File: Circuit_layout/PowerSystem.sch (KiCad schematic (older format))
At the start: 21 parts, among them U13 PDQ10-D, U14 PDQ15-D, U18 PDQ6-D

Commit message: fixed the throttle.
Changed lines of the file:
@@
 	5400 3650 5300 3650
 Wire Wire Line
-	5300 3550 5300 3650
-Wire Wire Line
-	4100 3550 5300 3550
+	5300 3650 5300 3550
+Wire Wire Line
+	5300 3550 4100 3550
 Connection ~ 4950 3550
 Connection ~ 4550 3550
@@
 	5400 3750 5300 3750
 Wire Wire Line
-	5300 3850 5300 3750
-Wire Wire Line
-	4100 3850 5300 3850
+	5300 3750 5300 3850
+Wire Wire Line
+	5300 3850 4100 3850
 Connection ~ 4950 3850
 Connection ~ 4550 3850
@@
 	5400 1600 5250 1600
 Wire Wire Line
-	5250 1550 5250 1600
+	5250 1600 5250 1550
 Wire Wire Line
 	5400 1700 5250 1700
 Wire Wire Line
-	5250 1850 5250 1700
-Wire Wire Line
-	4100 1850 5250 1850
+	5250 1700 5250 1850
+Wire Wire Line
+	5250 1850 4100 1850
 Connection ~ 4900 1550
 Connection ~ 4900 1850
@@
 Connection ~ 4550 1550
 $Comp
-L +24V #PWR43
+L +24V #PWR044
 U 1 1 58AF1DB3
 P 4100 3550
-F 0 "#PWR43" H 4100 3400 50  0001 C CNN
+F 0 "#PWR044" H 4100 3400 50  0001 C CNN
 F 1 "+24V" H 4100 3690 50  0000 C CNN
 F 2 "" H 4100 3550 50  0000 C CNN
@@
 $EndComp
 $Comp
-L +24V #PWR42
+L +24V #PWR045
 U 1 1 58AF1DD3
 P 4100 1550
-F 0 "#PWR42" H 4100 1400 50  0001 C CNN
+F 0 "#PWR045" H 4100 1400 50  0001 C CNN
 F 1 "+24V" H 4100 1690 50  0000 C CNN
 F 2 "" H 4100 1550 50  0000 C CNN
@@
 	7300 1600 7300 1500
 $Comp
-L +5V #PWR45
+L +5V #PWR046
 U 1 1 58AF2067
 P 7300 1500
-F 0 "#PWR45" H 7300 1350 50  0001 C CNN
+F 0 "#PWR046" H 7300 1350 50  0001 C CNN
 F 1 "+5V" H 7300 1640 50  0000 C CNN
 F 2 "" H 7300 1500 50  0000 C CNN
@@
 $EndComp
 $Comp
-L +12V #PWR47
+L +12V #PWR047
 U 1 1 58AF208D
 P 7350 3550
-F 0 "#PWR47" H 7350 3400 50  0001 C CNN
+F 0 "#PWR047" H 7350 3400 50  0001 C CNN
 F 1 "+12V" H 7350 3690 50  0000 C CNN
 F 2 "" H 7350 3550 50  0000 C CNN
@@
 	7300 1800 7300 1900
 $Comp
-L GND #PWR46
+L GND #PWR048
 U 1 1 58AF2561
 P 7300 1900
-F 0 "#PWR46" H 7300 1650 50  0001 C CNN
+F 0 "#PWR048" H 7300 1650 50  0001 C CNN
 F 1 "GND" H 7300 1750 50  0000 C CNN
 F 2 "" H 7300 1900 50  0000 C CNN
@@
 	7350 3850 7350 4000
 $Comp
-L GND #PWR48
+L GND #PWR049
 U 1 1 58AF25AA
 P 7350 4000
-F 0 "#PWR48" H 7350 3750 50  0001 C CNN
+F 0 "#PWR049" H 7350 3750 50  0001 C CNN
 F 1 "GND" H 7350 3850 50  0000 C CNN
 F 2 "" H 7350 4000 50  0000 C CNN
@@
 	4000 6900 3900 6900
 Wire Wire Line
-	3900 6800 3900 6900
-Wire Wire Line
-	3500 6800 3900 6800
+	3900 6900 3900 6800
+Wire Wire Line
+	3900 6800 3500 6800
 Connection ~ 3700 6800
 Connection ~ 3700 7100
@@
 LV_RTN
 $Comp
-L GND #PWR44
+L GND #PWR050
 U 1 1 58BA25F0
 P 6700 7250
-F 0 "#PWR44" H 6700 7000 50  0001 C CNN
+F 0 "#PWR050" H 6700 7000 50  0001 C CNN
 F 1 "GND" H 6700 7100 50  0000 C CNN
 F 2 "" H 6700 7250 50  0000 C CNN
@@
 	6700 7150 6700 7250
 Wire Wire Line
-	4100 1550 5250 1550
+	5250 1550 4100 1550
 Wire Notes Line
 	4750 6300 4750 7800
@@
 $EndComp
 $Comp
-L GND #PWR52
+L GND #PWR051
 U 1 1 58B9D18E
 P 7850 1950
-F 0 "#PWR52" H 7850 1700 50  0001 C CNN
+F 0 "#PWR051" H 7850 1700 50  0001 C CNN
 F 1 "GND" H 7850 1800 50  0000 C CNN
 F 2 "" H 7850 1950 50  0000 C CNN
@@
 $EndComp
 $Comp
-L +5V #PWR51
+L +5V #PWR052
 U 1 1 58B9D1D5
 P 7850 1450
-F 0 "#PWR51" H 7850 1300 50  0001 C CNN
+F 0 "#PWR052" H 7850 1300 50  0001 C CNN
 F 1 "+5V" H 7850 1590 50  0000 C CNN
 F 2 "" H 7850 1450 50  0000 C CNN
@@
 $EndComp
 $Comp
-L GND #PWR50
+L GND #PWR053
 U 1 1 58B9D3A5
 P 7750 4050
-F 0 "#PWR50" H 7750 3800 50  0001 C CNN
+F 0 "#PWR053" H 7750 3800 50  0001 C CNN
 F 1 "GND" H 7750 3900 50  0000 C CNN
 F 2 "" H 7750 4050 50  0000 C CNN
@@
 	7750 4050 7750 3950
 $Comp
-L +12V #PWR49
+L +12V #PWR054
 U 1 1 58B9D62A
 P 7750 3300
-F 0 "#PWR49" H 7750 3150 50  0001 C CNN
+F 0 "#PWR054" H 7750 3150 50  0001 C CNN
 F 1 "+12V" H 7750 3440 50  0000 C CNN
 F 2 "" H 7750 3300 50  0000 C CNN
@@
 $EndComp
 $Comp
-L PWR_FLAG #FLG3
+L PWR_FLAG #FLG055
 U 1 1 58B9E33D
 P 8150 3300
-F 0 "#FLG3" H 8150 3395 50  0001 C CNN
+F 0 "#FLG055" H 8150 3395 50  0001 C CNN
 F 1 "PWR_FLAG" H 8150 3480 50  0000 C CNN
 F 2 "" H 8150 3300 50  0000 C CNN

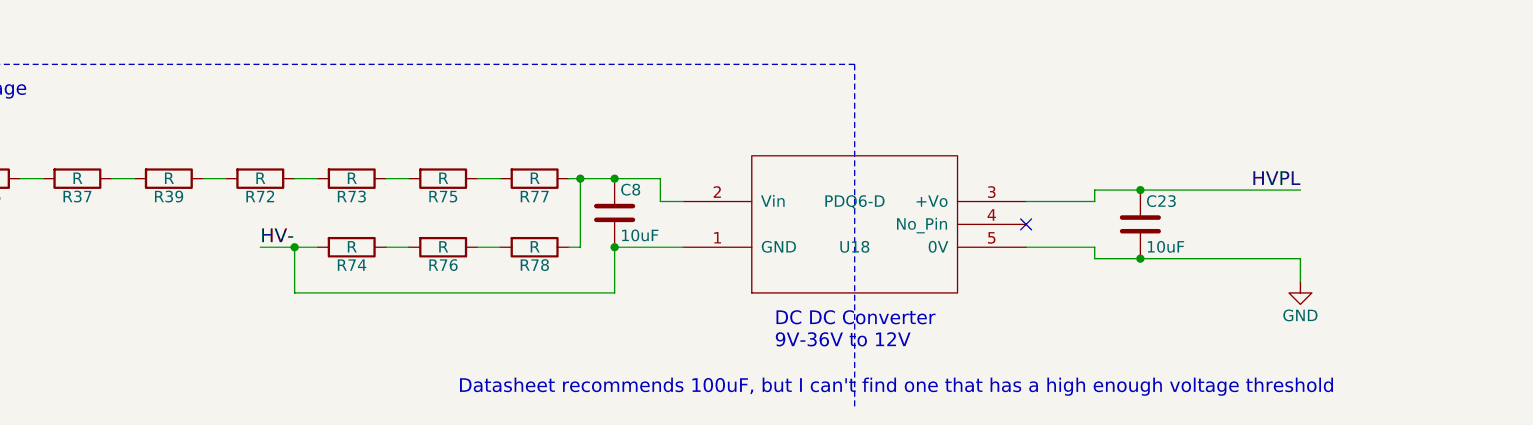
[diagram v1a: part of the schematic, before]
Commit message: added footprints
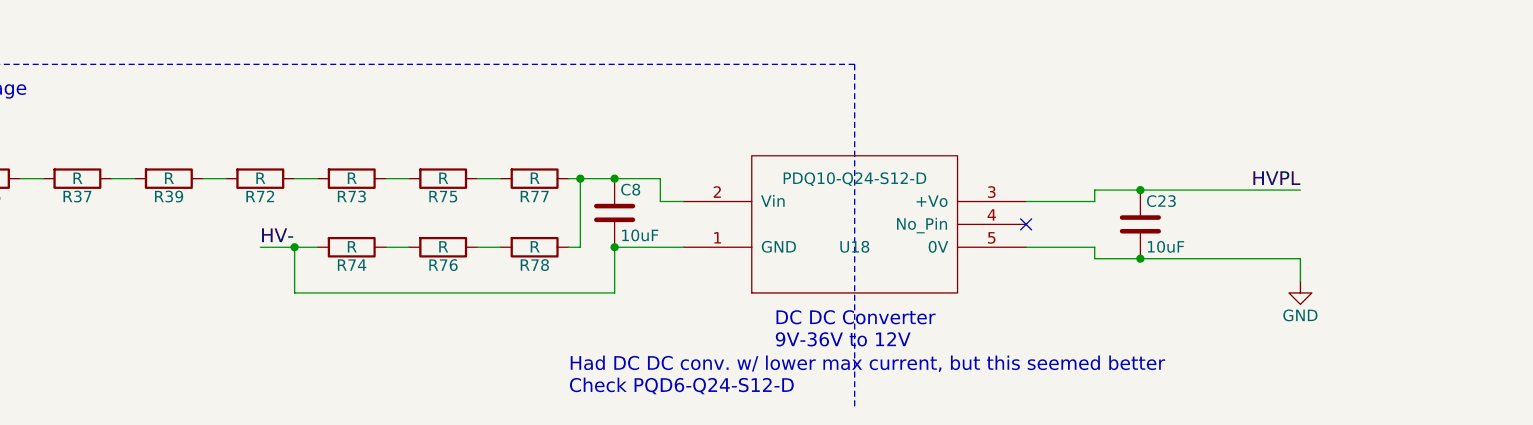
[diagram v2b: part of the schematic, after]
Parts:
- U13, U14: footprint (none) -> custom_footprints:PDQ_DCDC
- U18: value PDQ6-D -> PDQ10-Q24-S12-D; footprint (none) -> custom_footprints:PDQ_DCDC; DigiKey P/N  (none) -> 102-3866-ND; Man P/N (none) -> PDQ10-Q24-S12-D; URL (none) -> http://www.digikey.com/product-detail/en/cui-inc/PDQ10-Q24-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
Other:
- note added: "Had DC DC conv. w/ lower max current, but this seemed better\nCheck PQD6-Q24-S12-D"
- note removed: "Datasheet recommends 100uF, but I can't find one that has a high enough voltage threshold"
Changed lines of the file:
@@
 EESchema Schematic File Version 2
 LIBS:Circuit_layout-rescue
+LIBS:TSI_KiCad_Lib
 LIBS:TSI_HV_Isolater-cache
 LIBS:74xgxx
@@
 F 0 "U13" H 6150 1600 50  0000 C CNN
 F 1 "PDQ10-D" H 6150 1800 50  0000 C CNN
-F 2 "" H 6150 1300 50  0001 C CNN
+F 2 "custom_footprints:PDQ_DCDC" H 6150 1300 50  0001 C CNN
 F 3 "" H 6150 1200 50  0001 C CNN
 F 4 "	102-3865-ND" H 6150 1700 60  0001 C CNN "DigiKey P/N"
@@
 F 0 "U14" H 6150 3650 50  0000 C CNN
 F 1 "PDQ15-D" H 6150 3850 50  0000 C CNN
-F 2 "" H 6150 3350 50  0001 C CNN
+F 2 "custom_footprints:PDQ_DCDC" H 6150 3350 50  0001 C CNN
 F 3 "" H 6150 3250 50  0001 C CNN
 F 4 "102-3880-ND" H 6150 3750 60  0001 C CNN "DigiKey P/N"
@@
 Connection ~ 4550 1550
 $Comp
-L +24V #PWR044
+L +24V #PWR43
 U 1 1 58AF1DB3
 P 4100 3550
-F 0 "#PWR044" H 4100 3400 50  0001 C CNN
+F 0 "#PWR43" H 4100 3400 50  0001 C CNN
 F 1 "+24V" H 4100 3690 50  0000 C CNN
 F 2 "" H 4100 3550 50  0000 C CNN
@@
 $EndComp
 $Comp
-L +24V #PWR045
+L +24V #PWR42
 U 1 1 58AF1DD3
 P 4100 1550
-F 0 "#PWR045" H 4100 1400 50  0001 C CNN
+F 0 "#PWR42" H 4100 1400 50  0001 C CNN
 F 1 "+24V" H 4100 1690 50  0000 C CNN
 F 2 "" H 4100 1550 50  0000 C CNN
@@
 	7300 1600 7300 1500
 $Comp
-L +5V #PWR046
+L +5V #PWR45
 U 1 1 58AF2067
 P 7300 1500
-F 0 "#PWR046" H 7300 1350 50  0001 C CNN
+F 0 "#PWR45" H 7300 1350 50  0001 C CNN
 F 1 "+5V" H 7300 1640 50  0000 C CNN
 F 2 "" H 7300 1500 50  0000 C CNN
@@
 $EndComp
 $Comp
-L +12V #PWR047
+L +12V #PWR47
 U 1 1 58AF208D
 P 7350 3550
-F 0 "#PWR047" H 7350 3400 50  0001 C CNN
+F 0 "#PWR47" H 7350 3400 50  0001 C CNN
 F 1 "+12V" H 7350 3690 50  0000 C CNN
 F 2 "" H 7350 3550 50  0000 C CNN
@@
 	7300 1800 7300 1900
 $Comp
-L GND #PWR048
+L GND #PWR46
 U 1 1 58AF2561
 P 7300 1900
-F 0 "#PWR048" H 7300 1650 50  0001 C CNN
+F 0 "#PWR46" H 7300 1650 50  0001 C CNN
 F 1 "GND" H 7300 1750 50  0000 C CNN
 F 2 "" H 7300 1900 50  0000 C CNN
@@
 	7350 3850 7350 4000
 $Comp
-L GND #PWR049
+L GND #PWR48
 U 1 1 58AF25AA
 P 7350 4000
-F 0 "#PWR049" H 7350 3750 50  0001 C CNN
+F 0 "#PWR48" H 7350 3750 50  0001 C CNN
 F 1 "GND" H 7350 3850 50  0000 C CNN
 F 2 "" H 7350 4000 50  0000 C CNN
@@
 P 4750 7000
 F 0 "U18" H 4750 6900 50  0000 C CNN
-F 1 "PDQ6-D" H 4750 7100 50  0000 C CNN
-F 2 "" H 4750 6600 50  0001 C CNN
+F 1 "PDQ10-Q24-S12-D" H 4750 7200 50  0000 C CNN
+F 2 "custom_footprints:PDQ_DCDC" H 4750 6600 50  0001 C CNN
 F 3 "" H 4750 6500 50  0001 C CNN
+F 4 "102-3866-ND" H 4750 7000 60  0001 C CNN "DigiKey P/N "
+F 5 "http://www.digikey.com/product-detail/en/cui-inc/PDQ10-Q24-S12-D/102-3866-ND/6165207" H 4750 7000 60  0001 C CNN "URL"
+F 6 "PDQ10-Q24-S12-D" H 4750 7000 60  0001 C CNN "Man P/N"
 	1    4750 7000
 	1    0    0    -1
@@
 	1    0    0    -1
 $EndComp
-Text Notes 6850 7750 2    60   ~ 0
-Datasheet recommends 100uF, but I can't find one that has a high enough voltage threshold
+Text Notes 3500 7750 0    60   ~ 0
+Had DC DC conv. w/ lower max current, but this seemed better\nCheck PQD6-Q24-S12-D
 $Comp
 L C C10
@@
 LV_RTN
 $Comp
-L GND #PWR050
+L GND #PWR44
 U 1 1 58BA25F0
 P 6700 7250
-F 0 "#PWR050" H 6700 7000 50  0001 C CNN
+F 0 "#PWR44" H 6700 7000 50  0001 C CNN
 F 1 "GND" H 6700 7100 50  0000 C CNN
 F 2 "" H 6700 7250 50  0000 C CNN
@@
 $EndComp
 $Comp
-L GND #PWR051
+L GND #PWR52
 U 1 1 58B9D18E
 P 7850 1950
-F 0 "#PWR051" H 7850 1700 50  0001 C CNN
+F 0 "#PWR52" H 7850 1700 50  0001 C CNN
 F 1 "GND" H 7850 1800 50  0000 C CNN
 F 2 "" H 7850 1950 50  0000 C CNN
@@
 $EndComp
 $Comp
-L +5V #PWR052
+L +5V #PWR51
 U 1 1 58B9D1D5
 P 7850 1450
-F 0 "#PWR052" H 7850 1300 50  0001 C CNN
+F 0 "#PWR51" H 7850 1300 50  0001 C CNN
 F 1 "+5V" H 7850 1590 50  0000 C CNN
 F 2 "" H 7850 1450 50  0000 C CNN
@@
 $EndComp
 $Comp
-L GND #PWR053
+L GND #PWR50
 U 1 1 58B9D3A5
 P 7750 4050
-F 0 "#PWR053" H 7750 3800 50  0001 C CNN
+F 0 "#PWR50" H 7750 3800 50  0001 C CNN
 F 1 "GND" H 7750 3900 50  0000 C CNN
 F 2 "" H 7750 4050 50  0000 C CNN
@@
 	7750 4050 7750 3950
 $Comp
-L +12V #PWR054
+L +12V #PWR49
 U 1 1 58B9D62A
 P 7750 3300
-F 0 "#PWR054" H 7750 3150 50  0001 C CNN
+F 0 "#PWR49" H 7750 3150 50  0001 C CNN
 F 1 "+12V" H 7750 3440 50  0000 C CNN
 F 2 "" H 7750 3300 50  0000 C CNN
@@
 $EndComp
 $Comp
-L PWR_FLAG #FLG055
+L PWR_FLAG #FLG3
 U 1 1 58B9E33D
 P 8150 3300
-F 0 "#FLG055" H 8150 3395 50  0001 C CNN
+F 0 "#FLG3" H 8150 3395 50  0001 C CNN
 F 1 "PWR_FLAG" H 8150 3480 50  0000 C CNN
 F 2 "" H 8150 3300 50  0000 C CNN

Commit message: changing hvpl
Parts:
- removed R36, R37, R39, R72, R73, R74, R75, R76, R77, R78: R, symbol R
- added C?: 10uF, Capacitors_SMD:C_0805_HandSoldering, symbol C
- added L?: INDUCTOR, symbol INDUCTOR
- added R? (x4): R, symbol R
- added U?: LTC3638, custom_footprints:TSSOP16_LTC3638, symbol LTC3638
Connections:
- net HV+: now also C?.1, R?.1, U?.3 (Vin)
- net HV-: now also C?.2, R?.2, R?.2, U?.12 (OVLO), U?.16 (GND), U?.17 (GND), U?.6 (VPRG2), U?.8 (GND); no longer C8.2, U18.1 (GND)
- new net: C8.2, U18.1 (GND)
- new net: L?.1, U?.1 (SW)
- new net: U?.10 (SS), U?.7 (VPRG1)
- new net: R?.1, R?.2, U?.14 (RUN)
- new net: R?.1, R?.2, U?.9 (VFB)
- new net: L?.2, R?.1
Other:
- note removed: "Had DC DC conv. w/ lower max current, but this seemed better\nCheck PQD6-Q24-S12-D"
- moved on the sheet: C23, C8, U18

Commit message: made changes after init. review. Still need to add ports out of board.
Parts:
- gave numbers to parts that had none: 7
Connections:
- net HV+: no longer C19.1, R39.1, U16.3 (Vin)
- new net: C19.1, R39.1, U16.3 (Vin)
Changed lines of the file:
@@
 $EndComp
 $Comp
-L +24V #PWR43
+L +24V #PWR049
 U 1 1 58AF1DB3
 P 4100 3550
-F 0 "#PWR43" H 4100 3400 50  0001 C CNN
+F 0 "#PWR049" H 4100 3400 50  0001 C CNN
 F 1 "+24V" H 4100 3690 50  0000 C CNN
 F 2 "" H 4100 3550 50  0000 C CNN
@@
 $EndComp
 $Comp
-L +24V #PWR42
+L +24V #PWR050
 U 1 1 58AF1DD3
 P 4100 1550
-F 0 "#PWR42" H 4100 1400 50  0001 C CNN
+F 0 "#PWR050" H 4100 1400 50  0001 C CNN
 F 1 "+24V" H 4100 1690 50  0000 C CNN
 F 2 "" H 4100 1550 50  0000 C CNN
@@
 LVRTN
 $Comp
-L +5V #PWR45
+L +5V #PWR051
 U 1 1 58AF2067
 P 7300 1500
-F 0 "#PWR45" H 7300 1350 50  0001 C CNN
+F 0 "#PWR051" H 7300 1350 50  0001 C CNN
 F 1 "+5V" H 7300 1640 50  0000 C CNN
 F 2 "" H 7300 1500 50  0000 C CNN
@@
 $EndComp
 $Comp
-L +12V #PWR47
+L +12V #PWR052
 U 1 1 58AF208D
 P 7350 3550
-F 0 "#PWR47" H 7350 3400 50  0001 C CNN
+F 0 "#PWR052" H 7350 3400 50  0001 C CNN
 F 1 "+12V" H 7350 3690 50  0000 C CNN
 F 2 "" H 7350 3550 50  0000 C CNN
@@
 $EndComp
 $Comp
-L GND #PWR46
+L GND #PWR053
 U 1 1 58AF2561
 P 7300 1900
-F 0 "#PWR46" H 7300 1650 50  0001 C CNN
+F 0 "#PWR053" H 7300 1650 50  0001 C CNN
 F 1 "GND" H 7300 1750 50  0000 C CNN
 F 2 "" H 7300 1900 50  0000 C CNN
@@
 $EndComp
 $Comp
-L GND #PWR48
+L GND #PWR054
 U 1 1 58AF25AA
 P 7350 4000
-F 0 "#PWR48" H 7350 3750 50  0001 C CNN
+F 0 "#PWR054" H 7350 3750 50  0001 C CNN
 F 1 "GND" H 7350 3850 50  0000 C CNN
 F 2 "" H 7350 4000 50  0000 C CNN
@@
 LV_RTN
 $Comp
-L GND #PWR44
+L GND #PWR055
 U 1 1 58BA25F0
 P 6850 5800
-F 0 "#PWR44" H 6850 5550 50  0001 C CNN
+F 0 "#PWR055" H 6850 5550 50  0001 C CNN
 F 1 "GND" H 6850 5650 50  0000 C CNN
 F 2 "" H 6850 5800 50  0000 C CNN
@@
 $EndComp
 $Comp
-L GND #PWR52
+L GND #PWR056
 U 1 1 58B9D18E
 P 7850 1950
-F 0 "#PWR52" H 7850 1700 50  0001 C CNN
+F 0 "#PWR056" H 7850 1700 50  0001 C CNN
 F 1 "GND" H 7850 1800 50  0000 C CNN
 F 2 "" H 7850 1950 50  0000 C CNN
@@
 $EndComp
 $Comp
-L +5V #PWR51
+L +5V #PWR057
 U 1 1 58B9D1D5
 P 7850 1450
-F 0 "#PWR51" H 7850 1300 50  0001 C CNN
+F 0 "#PWR057" H 7850 1300 50  0001 C CNN
 F 1 "+5V" H 7850 1590 50  0000 C CNN
 F 2 "" H 7850 1450 50  0000 C CNN
@@
 $EndComp
 $Comp
-L GND #PWR50
+L GND #PWR058
 U 1 1 58B9D3A5
 P 7750 4050
-F 0 "#PWR50" H 7750 3800 50  0001 C CNN
+F 0 "#PWR058" H 7750 3800 50  0001 C CNN
 F 1 "GND" H 7750 3900 50  0000 C CNN
 F 2 "" H 7750 4050 50  0000 C CNN
@@
 $EndComp
 $Comp
-L +12V #PWR49
+L +12V #PWR059
 U 1 1 58B9D62A
 P 7750 3300
-F 0 "#PWR49" H 7750 3150 50  0001 C CNN
+F 0 "#PWR059" H 7750 3150 50  0001 C CNN
 F 1 "+12V" H 7750 3440 50  0000 C CNN
 F 2 "" H 7750 3300 50  0000 C CNN
@@
 $EndComp
 $Comp
-L PWR_FLAG #FLG3
+L PWR_FLAG #FLG060
 U 1 1 58B9E33D
 P 8150 3300
-F 0 "#FLG3" H 8150 3395 50  0001 C CNN
+F 0 "#FLG060" H 8150 3395 50  0001 C CNN
 F 1 "PWR_FLAG" H 8150 3480 50  0000 C CNN
 F 2 "" H 8150 3300 50  0000 C CNN
@@
 +24V_RTN
 $Comp
-L LTC3638 U?
+L LTC3638 U16
 U 1 1 58B9E882
 P 2350 6300
-F 0 "U?" H 2350 6450 60  0000 C CNN
+F 0 "U16" H 2350 6450 60  0000 C CNN
 F 1 "LTC3638" H 2350 6300 60  0000 C CNN
 F 2 "custom_footprints:TSSOP16_LTC3638" H 2350 6300 60  0001 C CNN
@@
 $EndComp
 $Comp
-L R R?
+L R R39
 U 1 1 58B9F3C1
 P 1150 6200
-F 0 "R?" V 1230 6200 50  0000 C CNN
+F 0 "R39" V 1230 6200 50  0000 C CNN
 F 1 "R" V 1150 6200 50  0000 C CNN
 F 2 "" V 1080 6200 50  0000 C CNN
@@
 Connection ~ 1700 6600
 $Comp
-L R R?
+L R R42
 U 1 1 58BABA72
 P 1150 6650
-F 0 "R?" V 1230 6650 50  0000 C CNN
+F 0 "R42" V 1230 6650 50  0000 C CNN
 F 1 "R" V 1150 6650 50  0000 C CNN
 F 2 "" V 1080 6650 50  0000 C CNN
@@
 $EndComp
 Wire Wire Line
-	600  6000 1850 6000
-Wire Wire Line
 	1150 6350 1150 6500
 Wire Wire Line
@@
 	2850 6000 3000 6000
 $Comp
-L INDUCTOR L?
+L INDUCTOR L1
 U 1 1 58BABEE0
 P 3300 6000
-F 0 "L?" V 3250 6000 50  0000 C CNN
+F 0 "L1" V 3250 6000 50  0000 C CNN
 F 1 "INDUCTOR" V 3400 6000 50  0000 C CNN
 F 2 "" H 3300 6000 50  0000 C CNN
@@
 	3600 6000 3750 6000
 $Comp
-L R R?
+L R R43
 U 1 1 58BABFDD
 P 3750 6250
-F 0 "R?" V 3830 6250 50  0000 C CNN
+F 0 "R43" V 3830 6250 50  0000 C CNN
 F 1 "R" V 3750 6250 50  0000 C CNN
 F 2 "" V 3680 6250 50  0000 C CNN
@@
 $EndComp
 $Comp
-L R R?
+L R R44
 U 1 1 58BAC057
 P 3750 6650
-F 0 "R?" V 3830 6650 50  0000 C CNN
+F 0 "R44" V 3830 6650 50  0000 C CNN
 F 1 "R" V 3750 6650 50  0000 C CNN
 F 2 "" V 3680 6650 50  0000 C CNN
@@
 	3750 6900 3750 6800
 $Comp
-L C C?
+L C C19
 U 1 1 58BAC255
 P 850 6450
-F 0 "C?" H 875 6550 50  0000 L CNN
+F 0 "C19" H 875 6550 50  0000 L CNN
 F 1 "10uF" H 875 6350 50  0000 L CNN
 F 2 "Capacitors_SMD:C_0805_HandSoldering" H 888 6300 50  0001 C CNN
@@
 Text Label 600  6900 0    60   ~ 0
 HV-
+Wire Wire Line
+	850  6000 1850 6000
+$Comp
+L PWR_FLAG #FLG061
+U 1 1 58BDEEDB
+P 1600 5900
+F 0 "#FLG061" H 1600 5995 50  0001 C CNN
+F 1 "PWR_FLAG" H 1600 6080 50  0000 C CNN
+F 2 "" H 1600 5900 50  0000 C CNN
+F 3 "" H 1600 5900 50  0000 C CNN
+	1    1600 5900
+	1    0    0    -1
+$EndComp
+Wire Wire Line
+	1600 5900 1600 6000
+Connection ~ 1600 6000
 $EndSCHEMATC

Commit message: updating HVPL schematic
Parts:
- removed C19, C23, C8: 10uF, Capacitors_SMD:C_0805_HandSoldering, symbol C
- removed L1: INDUCTOR, symbol INDUCTOR
- removed R39, R42, R43, R44: R, symbol R
- removed U16: LTC3638, custom_footprints:TSSOP16_LTC3638, symbol LTC3638
- removed U18: PDQ10-Q24-S12-D, custom_footprints:PDQ_DCDC, symbol PDQ6-D
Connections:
- no-connect marks 5 -> 4
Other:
- note removed: "High Voltage"
- moved on the sheet: C10, C11, C21, C36, C37, C9, U13, U14

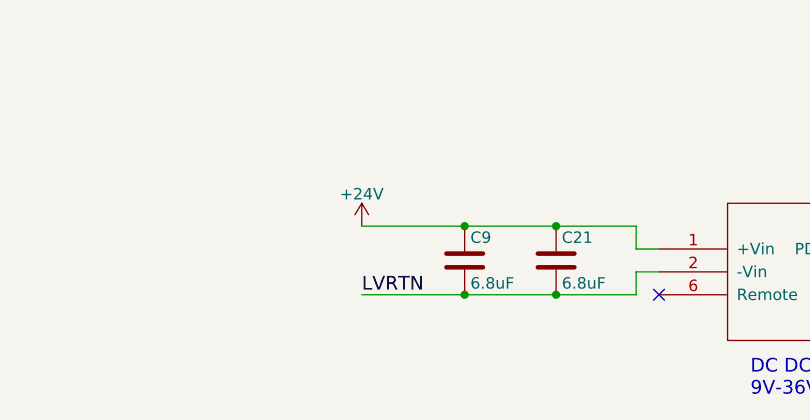
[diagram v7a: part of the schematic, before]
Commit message: Started PCB. Small changes to schematic. Adding system states visio file
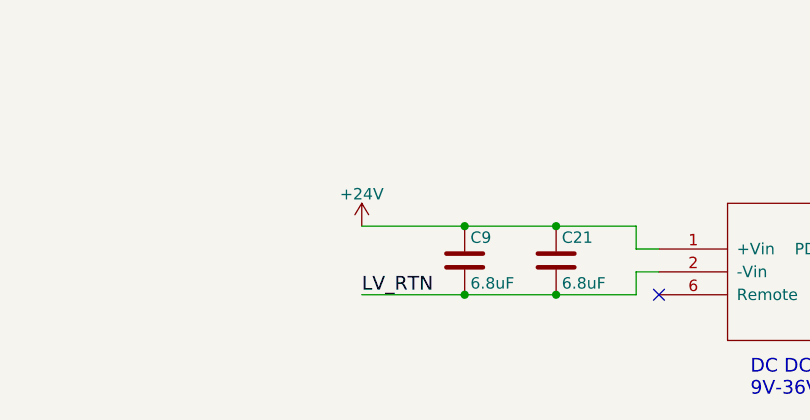
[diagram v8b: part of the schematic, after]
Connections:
- net LVRTN is gone; now on net +24V_RTN: C21.2, C9.2, U14.2 (-Vin)
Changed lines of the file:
@@
 $EndComp
 $Comp
-L +24V #PWR049
+L +24V #PWR052
 U 1 1 58AF1DB3
 P 3150 4350
-F 0 "#PWR049" H 3150 4200 50  0001 C CNN
+F 0 "#PWR052" H 3150 4200 50  0001 C CNN
 F 1 "+24V" H 3150 4490 50  0000 C CNN
 F 2 "" H 3150 4350 50  0000 C CNN
@@
 $EndComp
 $Comp
-L +24V #PWR050
+L +24V #PWR053
 U 1 1 58AF1DD3
 P 3150 2350
-F 0 "#PWR050" H 3150 2200 50  0001 C CNN
+F 0 "#PWR053" H 3150 2200 50  0001 C CNN
 F 1 "+24V" H 3150 2490 50  0000 C CNN
 F 2 "" H 3150 2350 50  0000 C CNN
@@
 LV_RTN
 Text Label 3150 4650 0    60   ~ 0
-LVRTN
-$Comp
-L +5V #PWR051
+LV_RTN
+$Comp
+L +5V #PWR054
 U 1 1 58AF2067
 P 6350 2300
-F 0 "#PWR051" H 6350 2150 50  0001 C CNN
+F 0 "#PWR054" H 6350 2150 50  0001 C CNN
 F 1 "+5V" H 6350 2440 50  0000 C CNN
 F 2 "" H 6350 2300 50  0000 C CNN
@@
 $EndComp
 $Comp
-L +12V #PWR052
+L +12V #PWR055
 U 1 1 58AF208D
 P 6400 4350
-F 0 "#PWR052" H 6400 4200 50  0001 C CNN
+F 0 "#PWR055" H 6400 4200 50  0001 C CNN
 F 1 "+12V" H 6400 4490 50  0000 C CNN
 F 2 "" H 6400 4350 50  0000 C CNN
@@
 $EndComp
 $Comp
-L GND #PWR053
+L GND #PWR056
 U 1 1 58AF2561
 P 6350 2700
-F 0 "#PWR053" H 6350 2450 50  0001 C CNN
+F 0 "#PWR056" H 6350 2450 50  0001 C CNN
 F 1 "GND" H 6350 2550 50  0000 C CNN
 F 2 "" H 6350 2700 50  0000 C CNN
@@
 $EndComp
 $Comp
-L GND #PWR054
+L GND #PWR057
 U 1 1 58AF25AA
 P 6400 4800
-F 0 "#PWR054" H 6400 4550 50  0001 C CNN
+F 0 "#PWR057" H 6400 4550 50  0001 C CNN
 F 1 "GND" H 6400 4650 50  0000 C CNN
 F 2 "" H 6400 4800 50  0000 C CNN
@@
 $EndComp
 $Comp
-L GND #PWR056
+L GND #PWR058
 U 1 1 58B9D18E
 P 6900 2750
-F 0 "#PWR056" H 6900 2500 50  0001 C CNN
+F 0 "#PWR058" H 6900 2500 50  0001 C CNN
 F 1 "GND" H 6900 2600 50  0000 C CNN
 F 2 "" H 6900 2750 50  0000 C CNN
@@
 $EndComp
 $Comp
-L +5V #PWR057
+L +5V #PWR059
 U 1 1 58B9D1D5
 P 6900 2250
-F 0 "#PWR057" H 6900 2100 50  0001 C CNN
+F 0 "#PWR059" H 6900 2100 50  0001 C CNN
 F 1 "+5V" H 6900 2390 50  0000 C CNN
 F 2 "" H 6900 2250 50  0000 C CNN
@@
 $EndComp
 $Comp
-L GND #PWR058
+L GND #PWR060
 U 1 1 58B9D3A5
 P 6800 4850
-F 0 "#PWR058" H 6800 4600 50  0001 C CNN
+F 0 "#PWR060" H 6800 4600 50  0001 C CNN
 F 1 "GND" H 6800 4700 50  0000 C CNN
 F 2 "" H 6800 4850 50  0000 C CNN
@@
 $EndComp
 $Comp
-L +12V #PWR059
+L +12V #PWR061
 U 1 1 58B9D62A
 P 6800 4100
-F 0 "#PWR059" H 6800 3950 50  0001 C CNN
+F 0 "#PWR061" H 6800 3950 50  0001 C CNN
 F 1 "+12V" H 6800 4240 50  0000 C CNN
 F 2 "" H 6800 4100 50  0000 C CNN
@@
 $EndComp
 $Comp
-L PWR_FLAG #FLG060
+L PWR_FLAG #FLG062
 U 1 1 58B9E33D
 P 7200 4100
-F 0 "#FLG060" H 7200 4195 50  0001 C CNN
+F 0 "#FLG062" H 7200 4195 50  0001 C CNN
 F 1 "PWR_FLAG" H 7200 4280 50  0000 C CNN
 F 2 "" H 7200 4100 50  0000 C CNN
